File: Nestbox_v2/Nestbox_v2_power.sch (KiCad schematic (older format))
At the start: 21 parts, among them J201 CONN_01X02, U201 TPS62745, U202 TPS62125, U203 LP5907

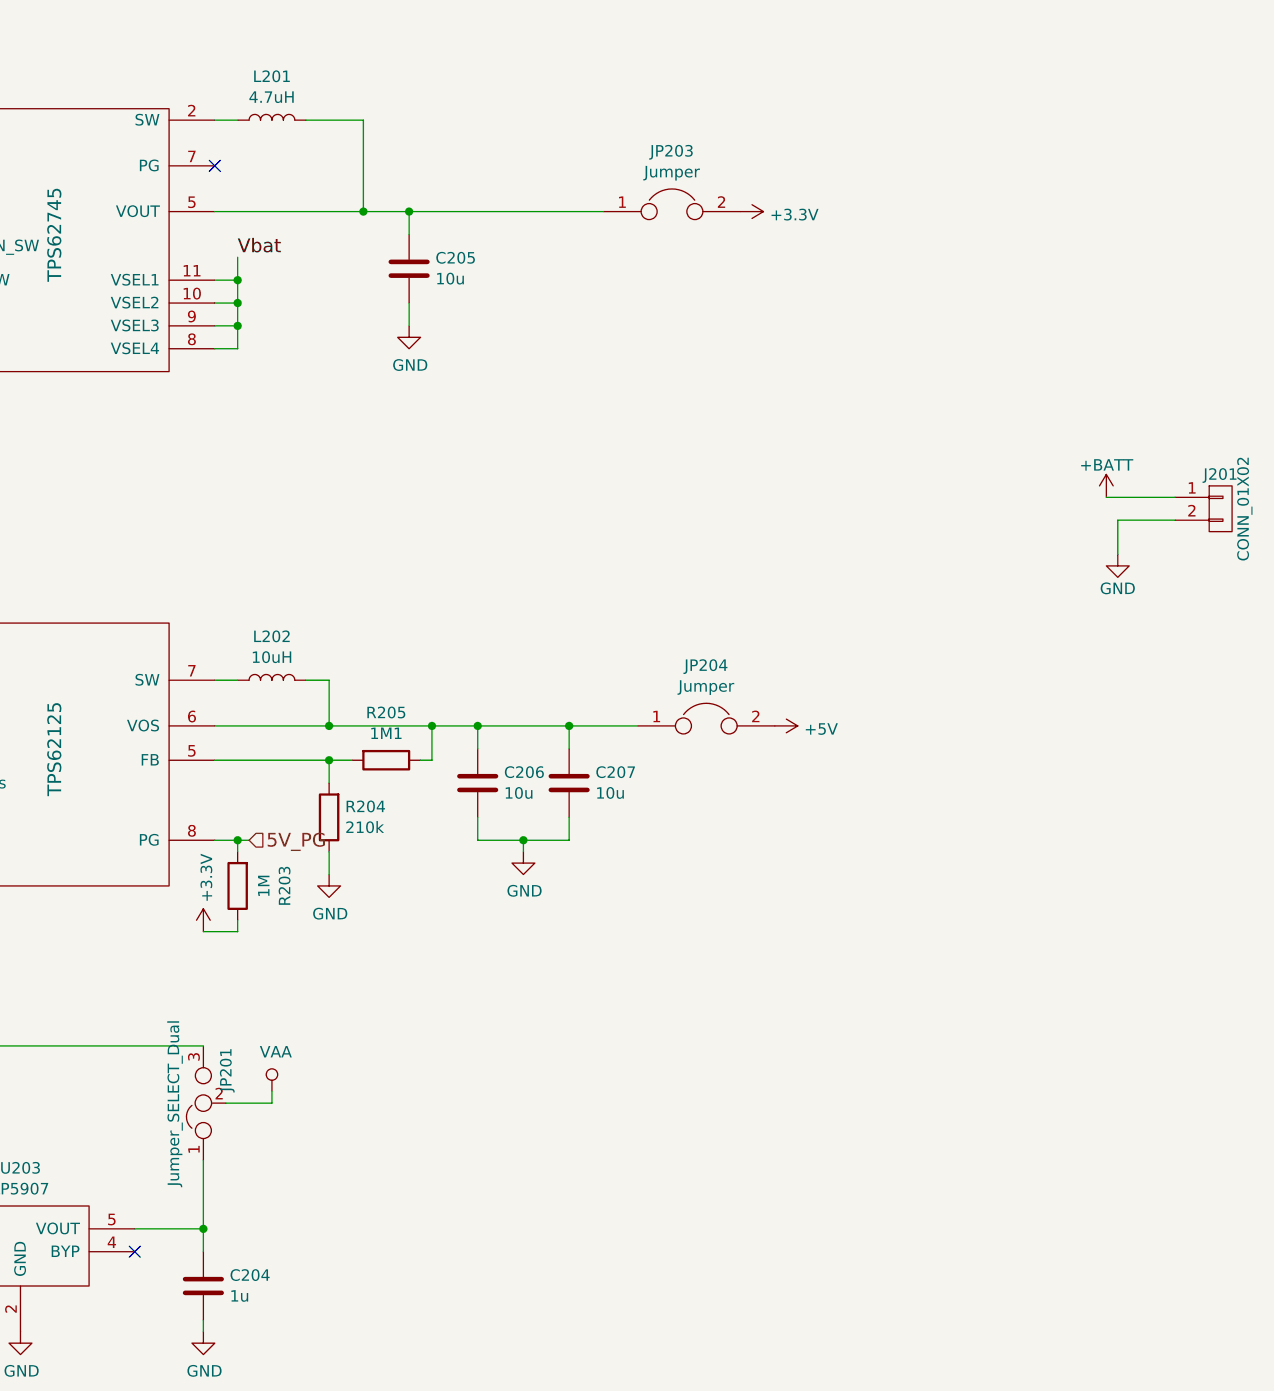
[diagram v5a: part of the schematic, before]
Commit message: correct size of the PCB drawn with connector arrangement done as well
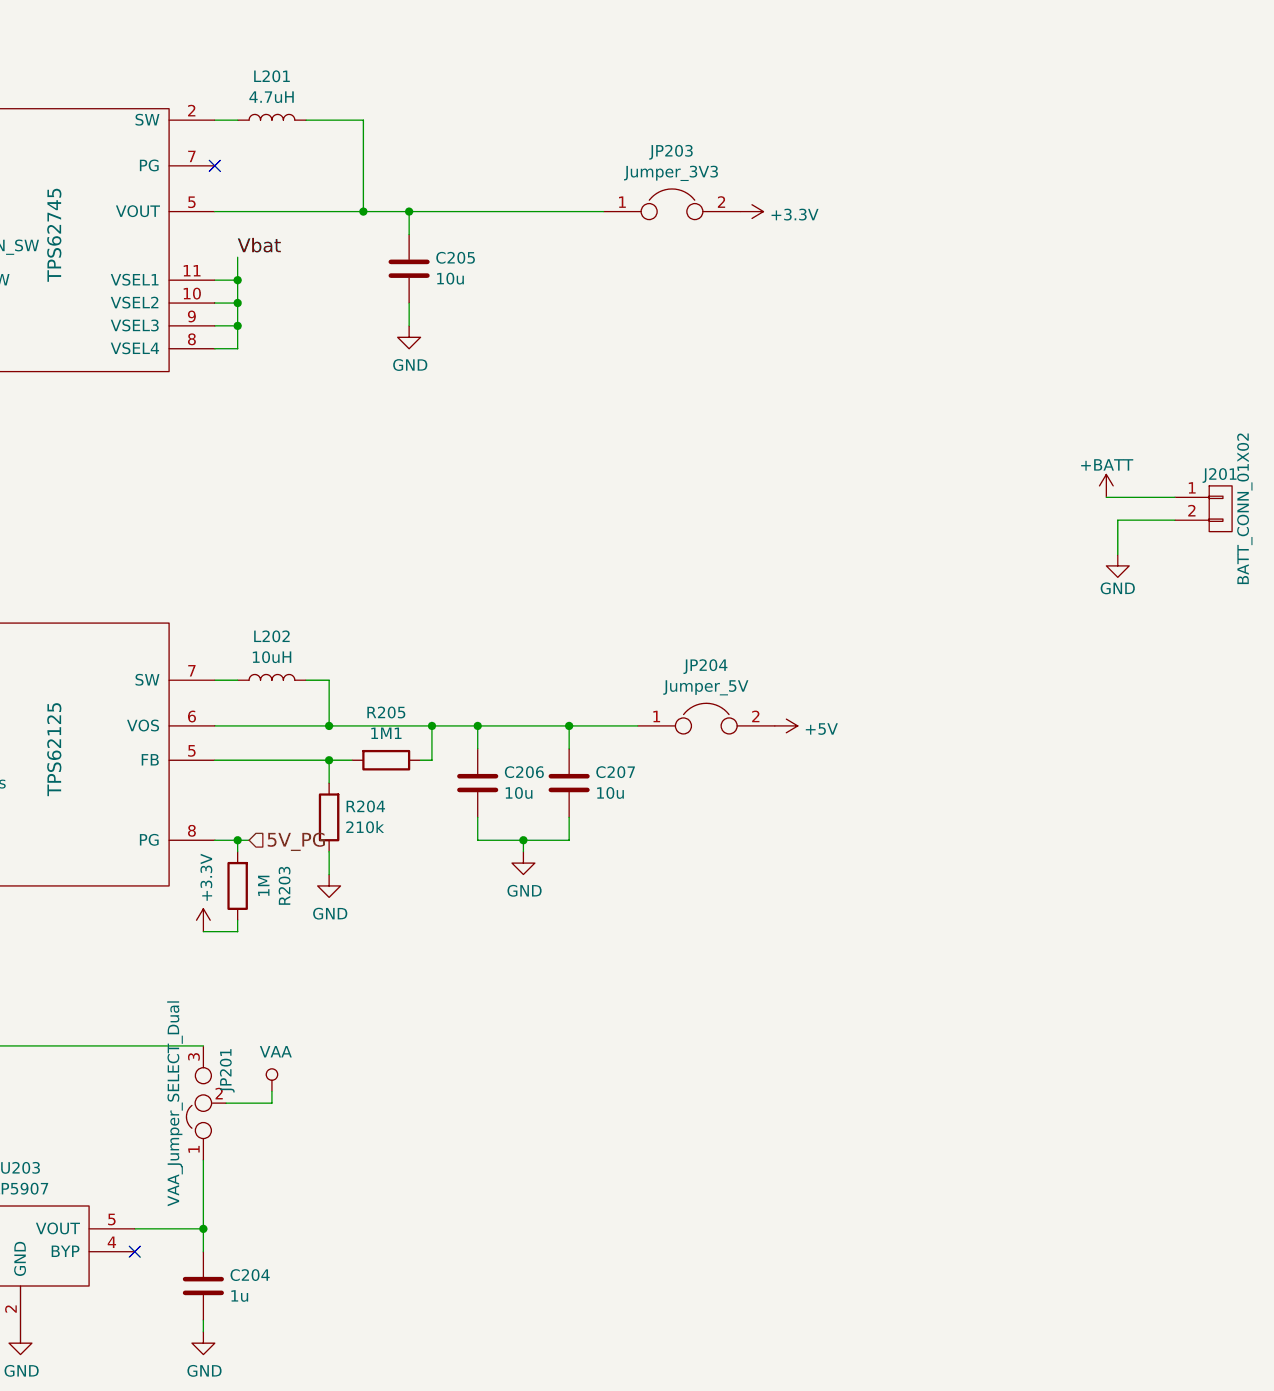
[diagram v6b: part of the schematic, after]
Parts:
- J201: value CONN_01X02 -> BATT_CONN_01X02
- JP201: value Jumper_SELECT_Dual -> VAA_Jumper_SELECT_Dual
- JP203: value Jumper -> Jumper_3V3
- JP204: value Jumper -> Jumper_5V
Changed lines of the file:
@@
 $EndComp
 $Comp
-L GND #PWR01
+L GND #PWR208
 U 1 1 5A0217A9
 P 3000 2550
-F 0 "#PWR01" H 3000 2300 50  0001 C CNN
+F 0 "#PWR208" H 3000 2300 50  0001 C CNN
 F 1 "GND" H 3005 2377 50  0000 C CNN
 F 2 "" H 3000 2550 50  0001 C CNN
@@
 $EndComp
 $Comp
-L GND #PWR02
+L GND #PWR203
 U 1 1 5A021A75
 P 1750 2400
-F 0 "#PWR02" H 1750 2150 50  0001 C CNN
+F 0 "#PWR203" H 1750 2150 50  0001 C CNN
 F 1 "GND" H 1755 2227 50  0000 C CNN
 F 2 "" H 1750 2400 50  0001 C CNN
@@
 $EndComp
 $Comp
-L +3.3V #PWR03
+L +3.3V #PWR217
 U 1 1 5A021DFB
 P 6750 1900
-F 0 "#PWR03" H 6750 1750 50  0001 C CNN
+F 0 "#PWR217" H 6750 1750 50  0001 C CNN
 F 1 "+3.3V" V 6765 2028 50  0000 L CNN
 F 2 "" H 6750 1900 50  0001 C CNN
@@
 $EndComp
 $Comp
-L GND #PWR04
+L GND #PWR209
 U 1 1 5A022A31
 P 3000 4800
-F 0 "#PWR04" H 3000 4550 50  0001 C CNN
+F 0 "#PWR209" H 3000 4550 50  0001 C CNN
 F 1 "GND" H 3005 4627 50  0000 C CNN
 F 2 "" H 3000 4800 50  0001 C CNN
@@
 $EndComp
 $Comp
-L GND #PWR05
+L GND #PWR207
 U 1 1 5A022A41
 P 2700 4650
-F 0 "#PWR05" H 2700 4400 50  0001 C CNN
+F 0 "#PWR207" H 2700 4400 50  0001 C CNN
 F 1 "GND" H 2705 4477 50  0000 C CNN
 F 2 "" H 2700 4650 50  0001 C CNN
@@
 $EndComp
 $Comp
-L +5V #PWR06
+L +5V #PWR218
 U 1 1 5A0232FE
 P 6900 4150
-F 0 "#PWR06" H 6900 4000 50  0001 C CNN
+F 0 "#PWR218" H 6900 4000 50  0001 C CNN
 F 1 "+5V" V 6915 4278 50  0000 L CNN
 F 2 "" H 6900 4150 50  0001 C CNN
@@
 $EndComp
 $Comp
-L GND #PWR07
+L GND #PWR216
 U 1 1 5A0246BF
 P 5800 4700
-F 0 "#PWR07" H 5800 4450 50  0001 C CNN
+F 0 "#PWR216" H 5800 4450 50  0001 C CNN
 F 1 "GND" H 5805 4527 50  0000 C CNN
 F 2 "" H 5800 4700 50  0001 C CNN
@@
 $EndComp
 $Comp
-L GND #PWR08
+L GND #PWR214
 U 1 1 5A0247CA
 P 4950 4800
-F 0 "#PWR08" H 4950 4550 50  0001 C CNN
+F 0 "#PWR214" H 4950 4550 50  0001 C CNN
 F 1 "GND" H 4955 4627 50  0000 C CNN
 F 2 "" H 4950 4800 50  0001 C CNN
@@
 $EndComp
 $Comp
-L GND #PWR09
+L GND #PWR215
 U 1 1 5A024E9A
 P 5300 2400
-F 0 "#PWR09" H 5300 2150 50  0001 C CNN
+F 0 "#PWR215" H 5300 2150 50  0001 C CNN
 F 1 "GND" H 5305 2227 50  0000 C CNN
 F 2 "" H 5300 2400 50  0001 C CNN
@@
 P 6600 4150
 F 0 "JP204" H 6600 4414 50  0000 C CNN
-F 1 "Jumper" H 6600 4323 50  0000 C CNN
+F 1 "Jumper_5V" H 6600 4323 50  0000 C CNN
 F 2 "Pin_Headers:Pin_Header_Straight_1x02" H 6600 4150 50  0001 C CNN
 F 3 "" H 6600 4150 50  0001 C CNN
@@
 P 6450 1900
 F 0 "JP203" H 6450 2164 50  0000 C CNN
-F 1 "Jumper" H 6450 2073 50  0000 C CNN
+F 1 "Jumper_3V3" H 6450 2073 50  0000 C CNN
 F 2 "Pin_Headers:Pin_Header_Straight_1x02" H 6450 1900 50  0001 C CNN
 F 3 "" H 6450 1900 50  0001 C CNN
@@
 P 8850 3200
 F 0 "J201" H 8850 3350 50  0000 C CNN
-F 1 "CONN_01X02" V 8950 3200 50  0000 C CNN
+F 1 "BATT_CONN_01X02" V 8950 3200 50  0000 C CNN
 F 2 "Terminal_Blocks:TerminalBlock_Pheonix_PT-3.5mm_2pol" H 8850 3200 50  0001 C CNN
 F 3 "" H 8850 3200 50  0001 C CNN
@@
 $EndComp
 $Comp
-L GND #PWR010
+L GND #PWR220
 U 1 1 5B072B3F
 P 8400 3400
-F 0 "#PWR010" H 8400 3150 50  0001 C CNN
+F 0 "#PWR220" H 8400 3150 50  0001 C CNN
 F 1 "GND" H 8400 3250 50  0000 C CNN
 F 2 "" H 8400 3400 50  0001 C CNN
@@
 $EndComp
 $Comp
-L +3V3 #PWR011
+L +3V3 #PWR204
 U 1 1 5B0757C4
 P 1950 6350
-F 0 "#PWR011" H 1950 6200 50  0001 C CNN
+F 0 "#PWR204" H 1950 6200 50  0001 C CNN
 F 1 "+3V3" H 1965 6523 50  0000 C CNN
 F 2 "" H 1950 6350 50  0001 C CNN
@@
 $EndComp
 $Comp
-L GND #PWR012
+L GND #PWR210
 U 1 1 5B0757CA
 P 3600 6800
-F 0 "#PWR012" H 3600 6550 50  0001 C CNN
+F 0 "#PWR210" H 3600 6550 50  0001 C CNN
 F 1 "GND" H 3605 6627 50  0000 C CNN
 F 2 "" H 3600 6800 50  0001 C CNN
@@
 NoConn ~ 4100 6450
 $Comp
-L VAA #PWR013
+L VAA #PWR213
 U 1 1 5B0757D1
 P 4700 5750
-F 0 "#PWR013" H 4700 5600 50  0001 C CNN
+F 0 "#PWR213" H 4700 5600 50  0001 C CNN
 F 1 "VAA" H 4717 5923 50  0000 C CNN
 F 2 "" H 4700 5750 50  0001 C CNN
@@
 $EndComp
 $Comp
-L +BATT #PWR014
+L +BATT #PWR201
 U 1 1 5B09033A
 P 700 1900
-F 0 "#PWR014" H 700 1750 50  0001 C CNN
+F 0 "#PWR201" H 700 1750 50  0001 C CNN
 F 1 "+BATT" H 700 2040 50  0000 C CNN
 F 2 "" H 700 1900 50  0001 C CNN
@@
 $EndComp
 $Comp
-L +BATT #PWR015
+L +BATT #PWR202
 U 1 1 5B090391
 P 1300 4150
-F 0 "#PWR015" H 1300 4000 50  0001 C CNN
+F 0 "#PWR202" H 1300 4000 50  0001 C CNN
 F 1 "+BATT" H 1300 4290 50  0000 C CNN
 F 2 "" H 1300 4150 50  0001 C CNN
@@
 $EndComp
 $Comp
-L GND #PWR016
+L GND #PWR206
 U 1 1 5B090D04
 P 2550 2950
-F 0 "#PWR016" H 2550 2700 50  0001 C CNN
+F 0 "#PWR206" H 2550 2700 50  0001 C CNN
 F 1 "GND" H 2555 2777 50  0000 C CNN
 F 2 "" H 2550 2950 50  0001 C CNN
@@
 $EndComp
 $Comp
-L +3.3V #PWR017
+L +3.3V #PWR211
 U 1 1 5B093809
 P 4400 5050
-F 0 "#PWR017" H 4400 4900 50  0001 C CNN
+F 0 "#PWR211" H 4400 4900 50  0001 C CNN
 F 1 "+3.3V" V 4415 5178 50  0000 L CNN
 F 2 "" H 4400 5050 50  0001 C CNN
@@
 $EndComp
 $Comp
-L GND #PWR018
+L GND #PWR205
 U 1 1 5B095296
 P 2500 6850
-F 0 "#PWR018" H 2500 6600 50  0001 C CNN
+F 0 "#PWR205" H 2500 6600 50  0001 C CNN
 F 1 "GND" H 2505 6677 50  0000 C CNN
 F 2 "" H 2500 6850 50  0001 C CNN
@@
 $EndComp
 $Comp
-L GND #PWR019
+L GND #PWR212
 U 1 1 5B095588
 P 4400 6800
-F 0 "#PWR019" H 4400 6550 50  0001 C CNN
+F 0 "#PWR212" H 4400 6550 50  0001 C CNN
 F 1 "GND" H 4405 6627 50  0000 C CNN
 F 2 "" H 4400 6800 50  0001 C CNN
@@
 $EndComp
 $Comp
-L +BATT #PWR020
+L +BATT #PWR219
 U 1 1 5B0B9A8C
 P 8350 3150
-F 0 "#PWR020" H 8350 3000 50  0001 C CNN
+F 0 "#PWR219" H 8350 3000 50  0001 C CNN
 F 1 "+BATT" H 8350 3290 50  0000 C CNN
 F 2 "" H 8350 3150 50  0001 C CNN
@@
 P 4400 5800
 F 0 "JP201" H 4450 5700 50  0000 L CNN
-F 1 "Jumper_SELECT_Dual" H 4400 5900 50  0000 C BNN
+F 1 "VAA_Jumper_SELECT_Dual" H 4400 5900 50  0000 C BNN
 F 2 "Pin_Headers:Pin_Header_Straight_1x03" H 4400 5800 50  0001 C CNN
 F 3 "" H 4400 5800 50  0001 C CNN

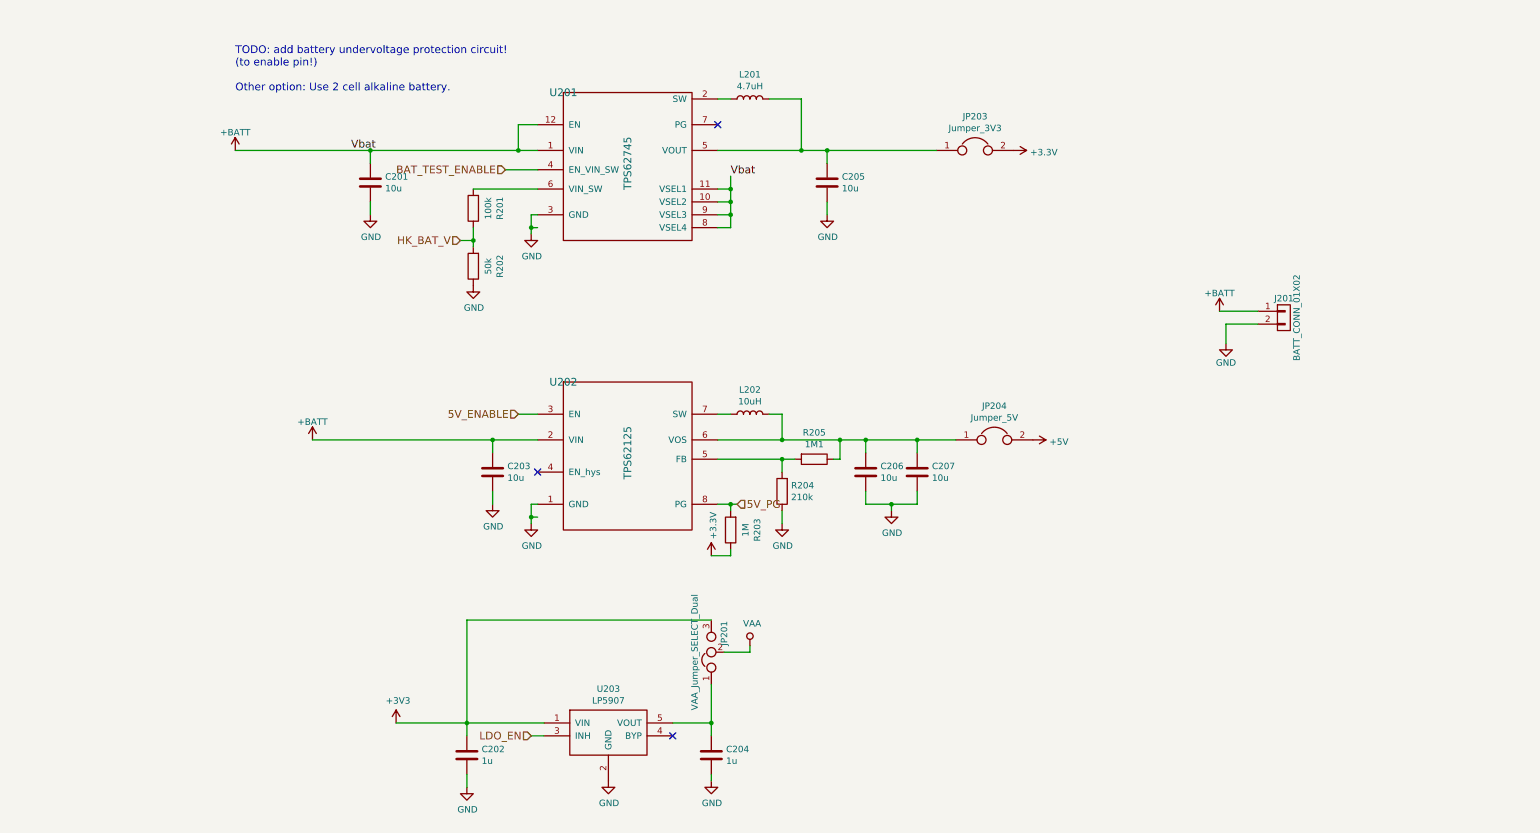
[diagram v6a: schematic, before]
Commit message: all footprints assigned except mosfets; final connectors and their locatino, started component placement
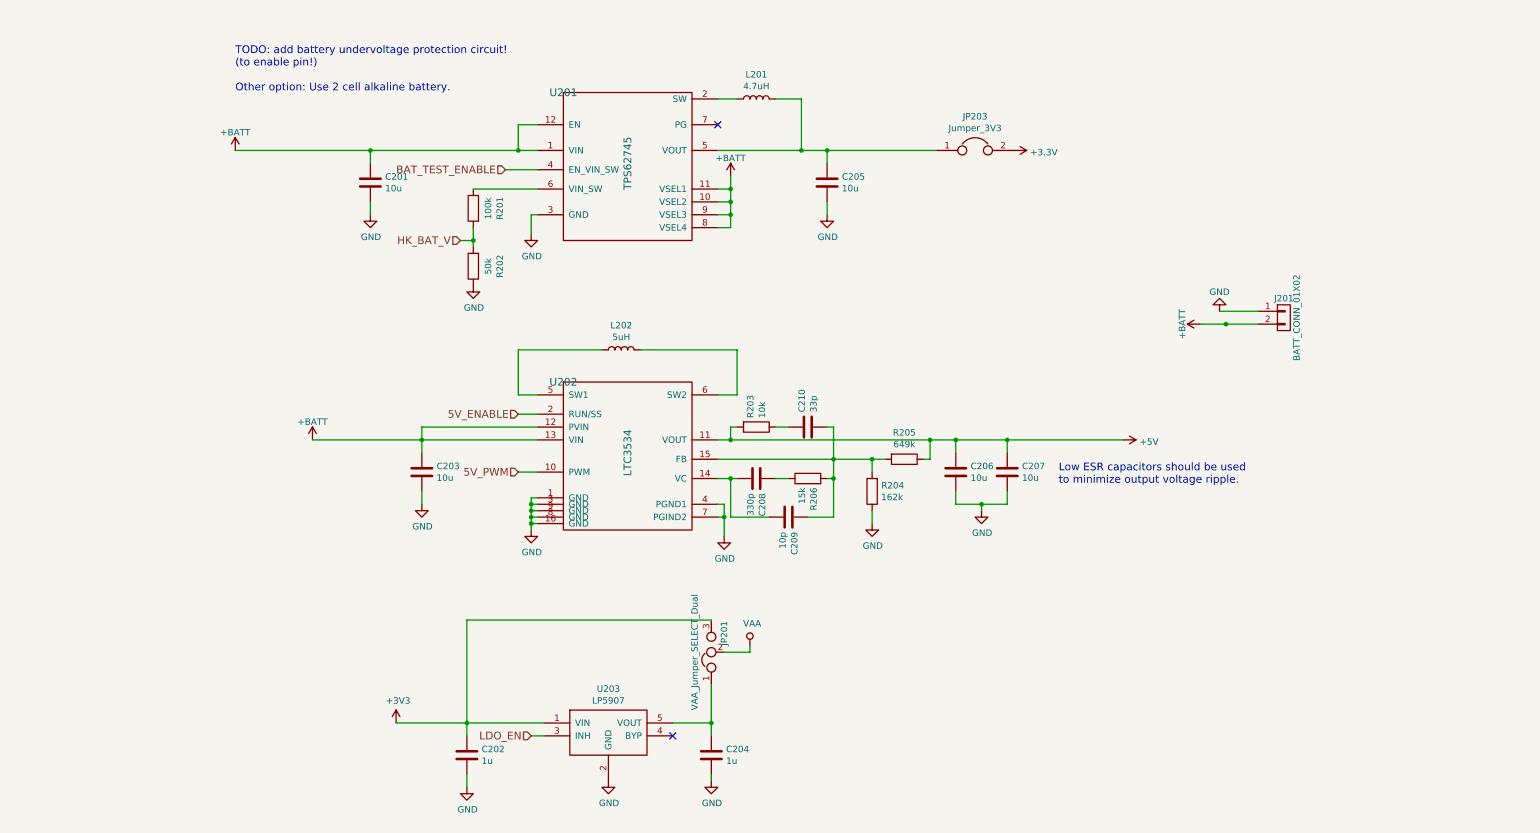
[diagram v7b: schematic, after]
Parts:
- removed JP204: Jumper_5V, Pin_Headers:Pin_Header_Straight_1x02, symbol Jumper
- removed U202: TPS62125, Octanis3:WSON_2x2mm_8pin, symbol TPS62125
- added C208: 330p, Capacitors_SMD:C_0603, symbol C
- added C209: 10p, Capacitors_SMD:C_0603, symbol C
- added C210: 33p, Capacitors_SMD:C_0603, symbol C
- added R206: 15k, Resistors_SMD:R_0603, symbol R
- added U202: LTC3534, SeeedOPL-IC-2016:SSOP16-0.635-5X4MM, symbol LTC3534
- L201: footprint (none) -> Inductors:Inductor_Taiyo-Yuden_NR-60xx_HandSoldering; MFG_PN (none) -> XFL3010-472MEB
- L202: value 10uH -> 5uH; footprint (none) -> Inductors:Inductor_Taiyo-Yuden_NR-30xx; MFR_PN (none) -> MSS7341-502NLD
- R203: value 1M -> 10k
- R204: value 210k -> 162k
- R205: value 1M1 -> 649k
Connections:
- net 5V_PG is gone; now on net +5V: R203.2
- net +3V3: no longer R203.1
- net +5V: now also C206.1, C207.1, R205.1, U202.11 (VOUT)
- net +BATT: now also J201.2 (P2), U202.12 (PVIN), U202.13 (VIN); no longer J201.1 (P1)
- net 5V_ENABLE: now also U202.2 (RUN/SS)
- net GND: now also J201.1 (P1), U202.1 (GND), U202.16 (GND), U202.3 (GND), U202.4 (PGND1), U202.7 (PGIND2), U202.8 (GND), U202.9 (GND); no longer J201.2 (P2)
- net at L202.1: now also U202.5 (SW1)
- net at R204.2, R205.2: now also C209.1, C210.2, R206.2, U202.15 (FB)
- new net: L202.2, U202.6 (SW2)
- new net: C208.2, C209.2, U202.14 (VC)
- new net: C210.1, R203.1
- new net: C208.1, R206.1
- new net 5V_PWM: U202.10 (PWM)
- no-connect marks 3 -> 2
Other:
- note added: "Low ESR capacitors should be used \nto minimize output voltage ripple. \n"
- moved on the sheet: C203, C206, C207, L201, L202, R204, R205
